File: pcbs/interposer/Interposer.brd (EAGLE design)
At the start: 100 x 100 mm, 28 parts

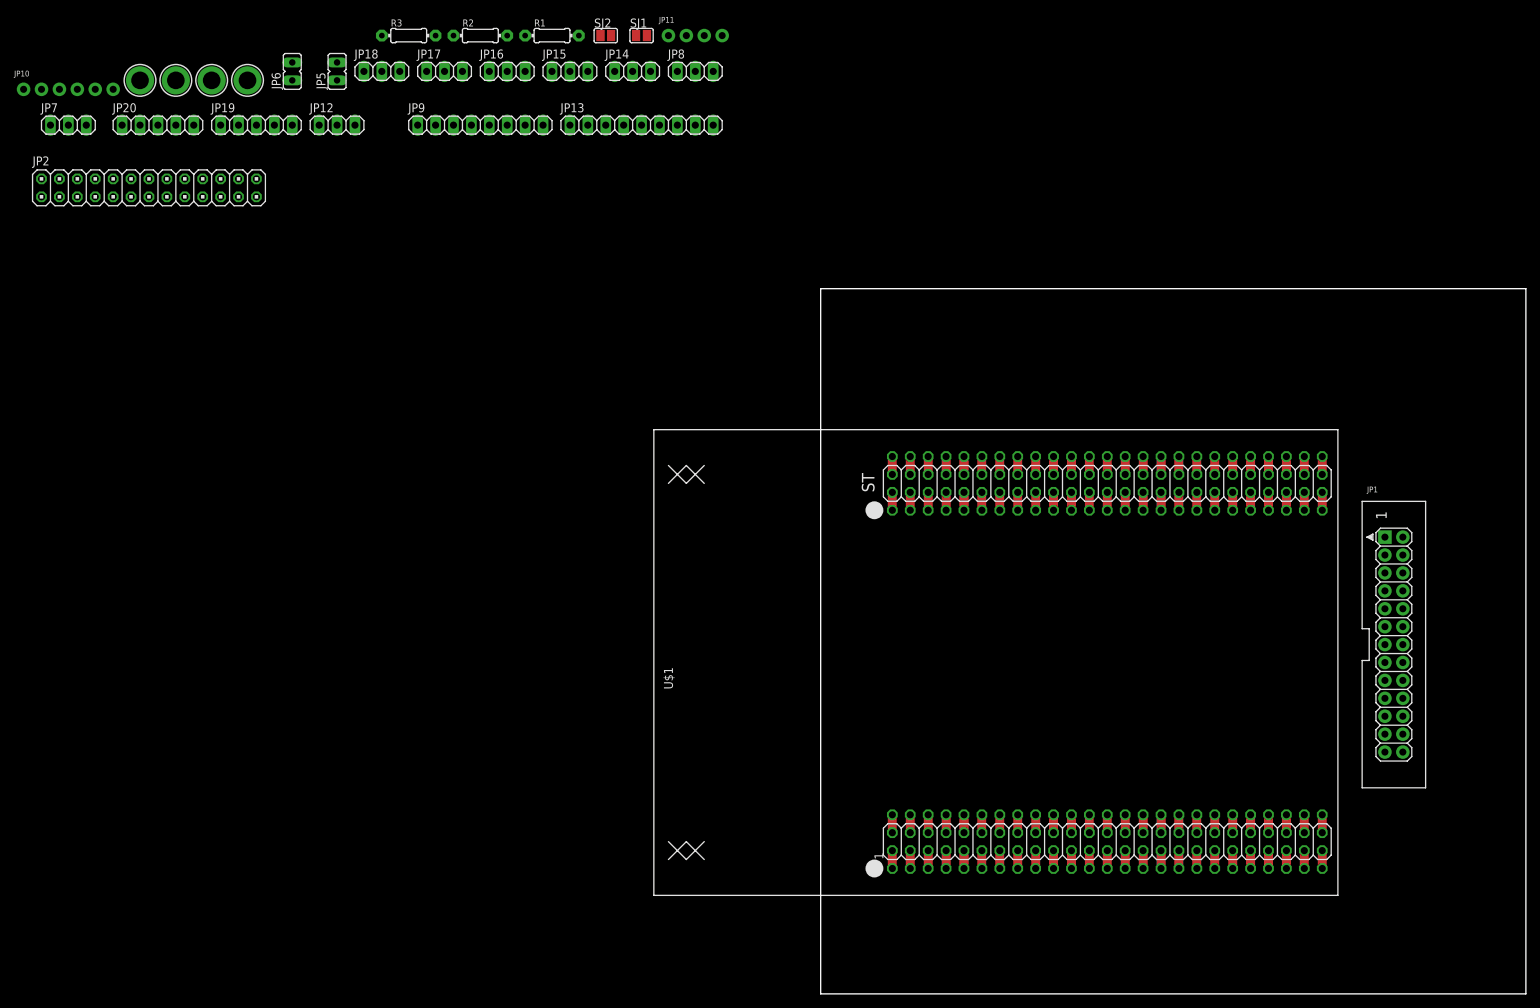
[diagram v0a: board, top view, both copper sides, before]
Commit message: Working through layout. Fixed a schematic bug and improved a few things.
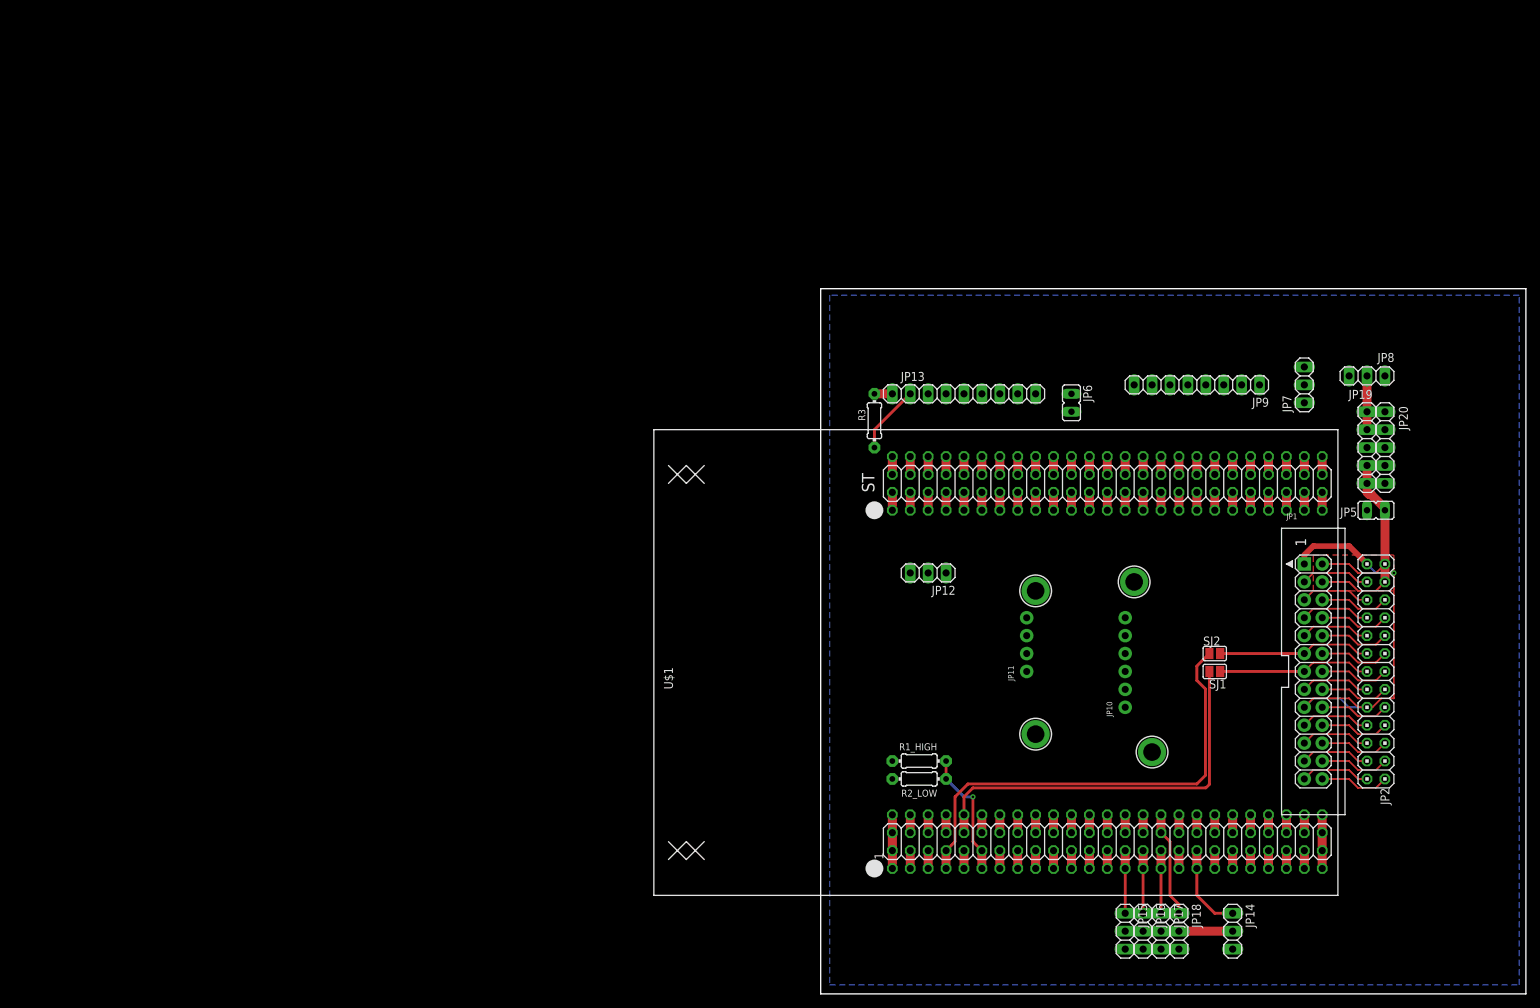
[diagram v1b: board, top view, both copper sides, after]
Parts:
- removed R1, R2: (no value), adafruit:0204/7
- added R1_HIGH, R2_LOW: (no value), adafruit:0204/7
- JP19: value POWproto -> RP,RP,ST,VI,VI
- JP5: value (none) -> RPi5V
- moved JP2 187.0 mm to (78.7, 45.7), turned to 270 degrees
- moved JP20 179.9 mm to (80.0, 77.5), turned to 90 degrees
- moved JP7 179.1 mm to (68.6, 86.4), turned to 90 degrees
- moved JP10 170.5 mm to (43.2, 47.0), turned to 90 degrees
- moved U$31 168.0 mm to (47.0, 34.3)
- moved JP18 166.3 mm to (50.8, 8.89), turned to 270 degrees
- moved JP19 164.0 mm to (77.5, 77.5), turned to 90 degrees
- moved JP5 159.9 mm to (78.7, 68.6), turned to 270 degrees
- moved JP17 158.7 mm to (48.3, 8.89), turned to 270 degrees
- moved U$32 157.2 mm to (30.5, 36.8)
- moved JP16 151.6 mm to (45.7, 8.89), turned to 270 degrees
- moved U$30 148.9 mm to (44.5, 58.4)
- moved JP14 148.7 mm to (58.4, 8.89), turned to 270 degrees
- moved JP15 145.1 mm to (43.2, 8.89), turned to 270 degrees
- moved U$29 133.2 mm to (30.5, 57.1)
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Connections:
- removed net +V: JP19.4, JP19.5, JP8.2
- removed net SERVO_SIG: U$1.195, U$1.90
- net +5V: now also JP19.4, JP19.5, JP8.2
- net BAT+: now also R1_HIGH.2; no longer R1.2
- net BATT_SENSE: now also R1_HIGH.1, R2_LOW.2; no longer R1.1, R2.2
- net CAM_SERVO: now also U$1.195, U$1.90
- net EGND: now also JP8.1, R2_LOW.1; no longer R2.1
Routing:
- net N$17: track 0.00 -> 66.0 mm
- net RPI_3V3: track 0.00 -> 58.1 mm, vias 0 -> 1
- net N$16: track 0.00 -> 56.6 mm
- net EGND: track 0.00 -> 54.8 mm
- net RPI_5V: track 0.00 -> 37.6 mm
- net +5V: track 0.00 -> 22.9 mm
- net RPI_GPIO_OUT: track 0.00 -> 21.9 mm
- net RPI_GPIO_IN: track 0.00 -> 21.9 mm
- net BATT_SENSE: track 0.00 -> 18.1 mm, vias 0 -> 1
- net TIM1_CH4: track 0.00 -> 15.0 mm
- net TIM2_CH4: track 0.00 -> 12.5 mm
- net N$4: track 0.00 -> 9.94 mm
- net RPI_TXD: track 0.00 -> 9.94 mm
- net N$14: track 0.00 -> 9.94 mm
- net N$13: track 0.00 -> 9.94 mm
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- added copper zone on layer 16, net EGND
- added copper zone on layer 1, net RPI_5V

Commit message: Finished interposer board.
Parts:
- added U$2, U$3, U$4, U$5: (no value), HighCurrentTransistorAndDriver:RPI_MOUNTING_HOLE
- JP12: value GPS_5Vsrc_sel -> GPS_5Vsrc
- JP14, JP15, JP16, JP17, JP18, JP7: device pinhead:1X03 -> Interposer:1X03
- JP19, JP20: device pinhead:1X05 -> Interposer:1X05
- JP6: value (none) -> STM_PWR
- moved JP7 81.9 mm to (55.1, 5.59), turned to 270 degrees
- moved U$31 28.0 mm to (29.7, 56.4), turned to 90 degrees
- moved JP12 23.6 mm to (28.4, 79.2), turned to 270 degrees
- moved U$29 22.4 mm to (29.7, 34.8), turned to 90 degrees
- moved U$32 14.6 mm to (45.0, 34.8), turned to 90 degrees
- moved JP13 7.84 mm to (13.2, 81.8)
- moved R3 7.42 mm to (3.05, 75.4)
- moved JP9 7.42 mm to (47.5, 81.8)
- moved JP14 6.71 mm to (52.6, 5.59)
- moved JP8 6.71 mm to (74.2, 81.8)
- moved JP20 4.67 mm to (76.7, 74.2)
- moved R1_HIGH 4.67 mm to (10.7, 29.7)
- moved JP6 4.67 mm to (32.3, 80.5)
- moved R2_LOW 4.67 mm to (10.7, 27.2)
- moved U$1 4.67 mm to (6.86, 17.0)
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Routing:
- net +5V: track 22.9 -> 165.1 mm
- net STM5V: track 0.00 -> 125.5 mm, vias 0 -> 1
- net BAT+: track 0.00 -> 96.7 mm, vias 0 -> 2
- net CAM_SERVO: track 0.00 -> 75.5 mm
- net RPI_TXD: track 9.94 -> 46.3 mm, vias 0 -> 2
- net ESTOP_L: track 0.00 -> 34.4 mm, vias 0 -> 1
- net RPI_RXD: track 9.94 -> 44.3 mm, vias 0 -> 2
- net BNO_SDA: track 0.00 -> 34.3 mm
- net GPS_RX: track 0.00 -> 34.3 mm, vias 0 -> 3
- net BNO_RST_L: track 0.00 -> 33.5 mm, vias 0 -> 2
- net GPS_TX: track 0.00 -> 32.3 mm, vias 0 -> 2
- net ESC3: track 0.00 -> 26.7 mm, vias 0 -> 2
- net ESC2: track 0.00 -> 26.7 mm, vias 0 -> 2
- net BNO_SCL: track 0.00 -> 26.4 mm
- net GPS_EN: track 9.72 -> 36.0 mm, vias 0 -> 1
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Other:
- board size 100 x 100 mm -> 79.5 x 86 mm
- board text added: "Adafruit BNO055 breakout"
- board text added: "Autonomous Facial Recognition Quadcopter"
- board text added: "Interposer board V1.0 Feb 16 2020"
- board text added: "RST"
- board text added: "VIN"

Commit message: Increased e-stop <-> interposer ribbon cable drill size to make soldering the ribbon cable easier in future versions.
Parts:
- JP9: device pinhead:1X08 -> HighCurrentTransistorAndDriver:1X08_RIBBONCABLE
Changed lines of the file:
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@@
 <attribute name="VALUE" x="74.17" y="84.965" size="1.27" layer="27" rot="R180"/>
 </element>
-<element name="JP9" library="pinhead" library_urn="urn:adsk.eagle:library:325" package="1X08" package3d_urn="urn:adsk.eagle:package:22409/2" value="EStopBrd_cable" x="47.5" y="81.79" smashed="yes" rot="R180">
+<element name="JP9" library="HighCurrentTransistorAndDriver" package="1X08_RIBBONCABLE" package3d_urn="urn:adsk.eagle:package:22409/2" value="EStopBrd_cable" x="47.5" y="81.79" smashed="yes" rot="R180">
 <attribute name="NAME" x="42.4962" y="85.0412" size="1.27" layer="25" ratio="10" rot="R180"/>
 <attribute name="POPULARITY" value="67" x="-0.76" y="204.98" size="1.778" layer="27" rot="R180" display="off"/>
